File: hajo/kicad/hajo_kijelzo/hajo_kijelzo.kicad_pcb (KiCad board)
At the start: 2 copper layers, 69.2 x 89.5 mm, 26 parts, among them J1 Seetalk NG, J2 Batteries, J3 Terminator, J4 Conn_01x14, Q1 BC557, U1 MCP2562, U2 LF50CV, U3 LF33_TO220

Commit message: fix boards
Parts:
- Q1: footprint Package_TO_SOT_THT:TO-92_Inline -> Package_TO_SOT_THT:TO-92_Inline_Wide
- moved H2 0.50 mm to (18.6, 93.4)
- moved H4 0.50 mm to (76.9, 93.4)
- moved H1 0.25 mm to (76.9, 21.6)
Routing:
- net +3.3V: track 72.8 -> 75.9 mm
- net /L_BACK: track 26.4 -> 23.9 mm
- net Net-(Q1-B): track 5.08 -> 5.61 mm
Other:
- outline, holes or cut-outs redrawn
- board text added: "+"

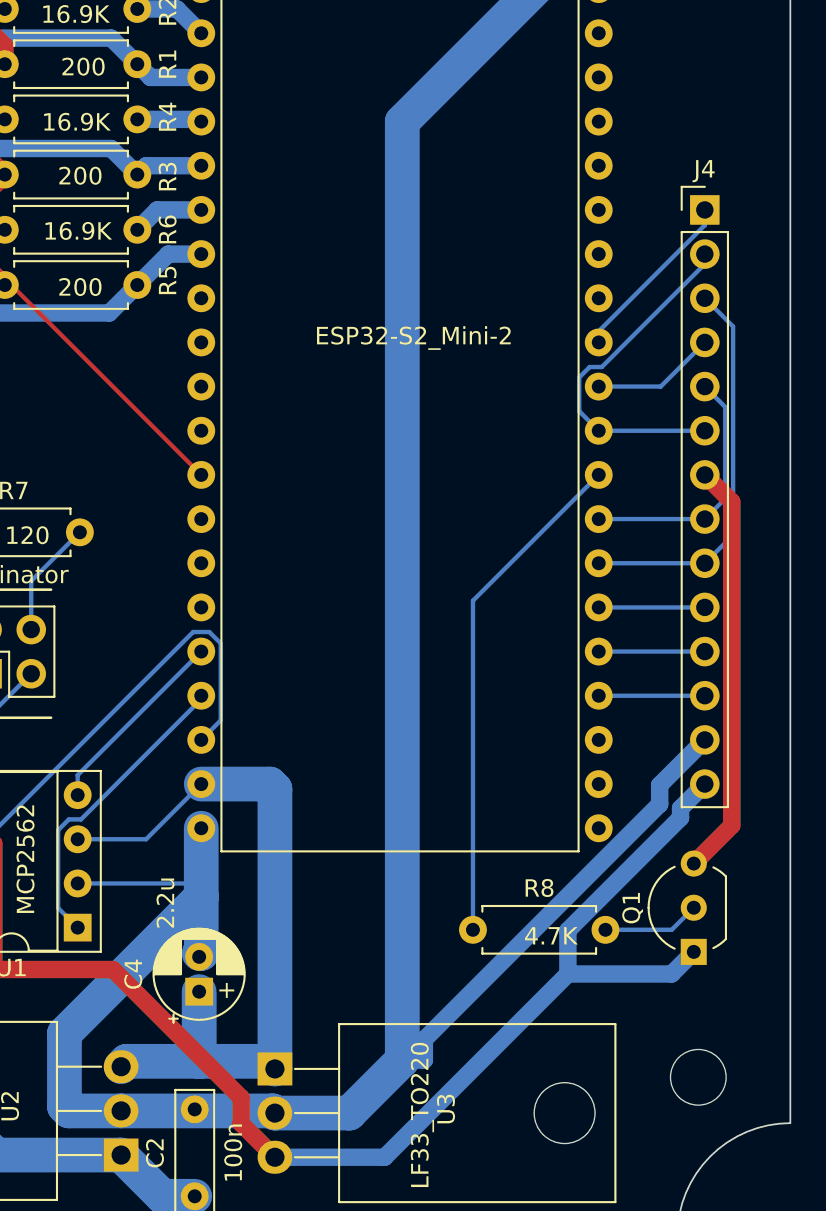
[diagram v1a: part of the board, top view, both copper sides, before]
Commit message: display pcb add capacitor, change R values
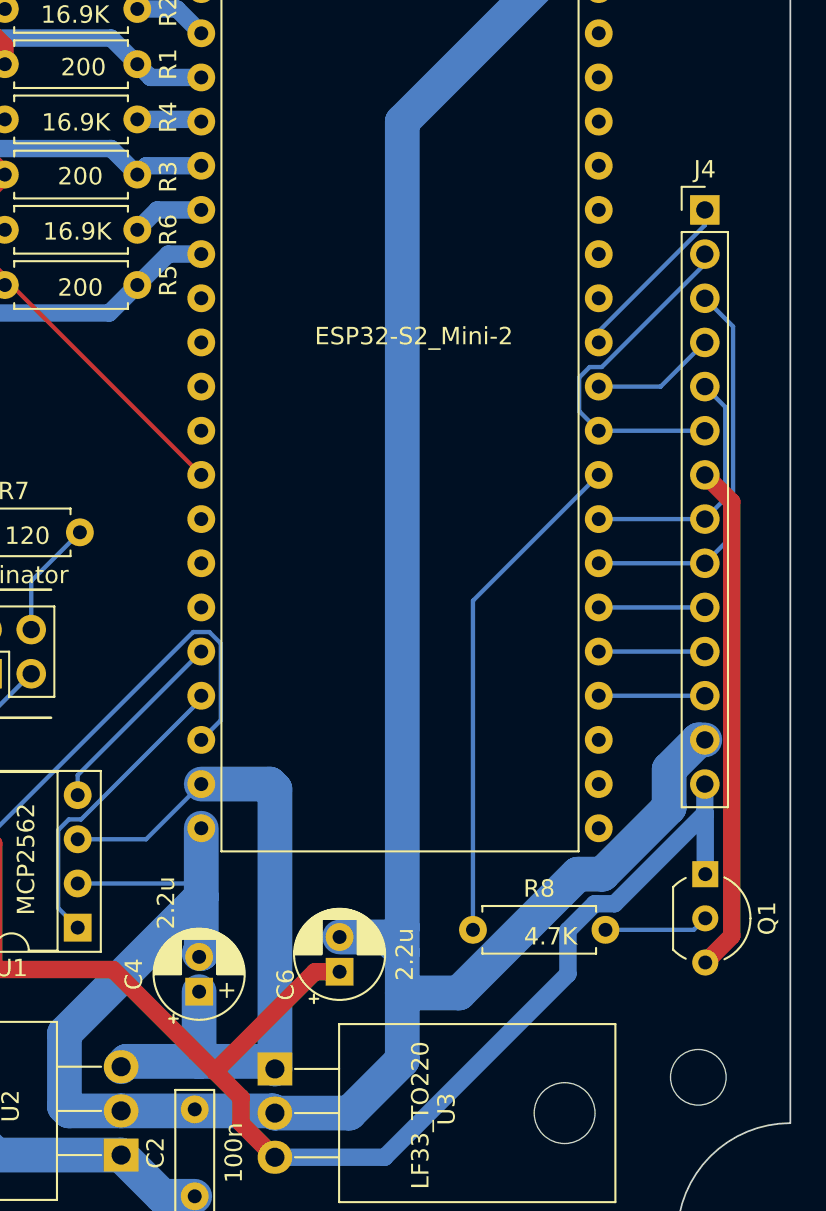
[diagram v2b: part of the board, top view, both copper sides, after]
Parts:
- added C6: 2.2u, Capacitor_THT:CP_Radial_D5.0mm_P2.00mm, F.Cu at (56.3, 87.3)
- moved Q1 4.52 mm to (77.3, 81.7), turned to -90 degrees
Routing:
- net +3.3V: track 75.9 -> 81.8 mm
- net /L_BACK: track 23.9 -> 29.3 mm
- net GND: track 288.3 -> 290.7 mm

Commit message: pcb changes
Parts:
- C1, C3, C5: footprint Capacitor_THT:C_Rect_L7.0mm_W2.0mm_P5.00mm -> Capacitor_THT:C_Rect_L4.0mm_W2.5mm_P2.50mm
- R1, R3, R5: value 200 -> 51.1
- R2, R4, R6: value 16.9K -> 806
- moved C1 5.68 mm to (34.0, 34.6)
- moved C3 5.63 mm to (34.1, 42.2)
- moved C5 5.46 mm to (34.1, 49.9)
- moved R5 4.95 mm to (37.1, 52.8)
- moved R6 4.95 mm to (44.7, 49.6)
- moved R4 3.64 mm to (44.6, 41.9)
- moved R3 3.64 mm to (37.0, 45.1)
- moved R1 2.29 mm to (36.9, 37.4)
- moved R2 2.29 mm to (44.5, 34.2)
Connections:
- A1 pad 10: unconnected-(A1-GPIO8/ADC1_7-Pad10) -> /ADC3_H
- A1 pad 11: unconnected-(A1-GPIO9/ADC1_8-Pad11) -> /ADC3_L
- A1 pad 4: /ADC1 -> /ADC1_H
- A1 pad 5: /DRV2 -> /ADC1_L
- A1 pad 6: /ADC2 -> /DRV2
- A1 pad 7: /DRV3 -> /ADC2_H
- A1 pad 8: /ADC3 -> /ADC2_L
- A1 pad 9: unconnected-(A1-GPIO7/ADC1_6-Pad9) -> /DRV3
- C1 pad 2: /ADC1 -> /ADC1_L
- C3 pad 2: /ADC2 -> /ADC2_L
- C5 pad 2: /ADC3 -> /ADC3_L
- J2 pad 1: /ADC3 -> /ADC3_L
- J2 pad 2: Net-(J2-Pin_2) -> /ADC3_H
- J2 pad 3: /ADC2 -> /ADC2_L
- J2 pad 4: Net-(J2-Pin_4) -> /ADC2_H
- J2 pad 5: /ADC1 -> /ADC1_L
- J2 pad 6: Net-(J2-Pin_6) -> /ADC1_H
- R1 pad 2: /ADC1 -> /ADC1_L
- R2 pad 2: Net-(J2-Pin_6) -> /ADC1_H
- R3 pad 2: /ADC2 -> /ADC2_L
- R4 pad 2: Net-(J2-Pin_4) -> /ADC2_H
- R5 pad 2: /ADC3 -> /ADC3_L
- R6 pad 2: Net-(J2-Pin_2) -> /ADC3_H
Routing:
- net /ADC3: track 24.7 -> 0.00 mm
- net /ADC3_L: track 0.00 -> 23.5 mm
- net /ADC2: track 23.5 -> 0.00 mm
- net /ADC1_L: track 0.00 -> 22.5 mm
- net /ADC2_L: track 0.00 -> 22.4 mm
- net /ADC3_H: track 0.00 -> 22.4 mm
- net /ADC1_H: track 0.00 -> 22.3 mm
- net /ADC1: track 22.0 -> 0.00 mm
- net /ADC2_H: track 0.00 -> 21.3 mm
- net Net-(J2-Pin_2): track 11.5 -> 0.00 mm
- net Net-(J2-Pin_4): track 9.94 -> 0.00 mm
- net Net-(J2-Pin_6): track 9.42 -> 0.00 mm
- net GND: track 290.7 -> 296.5 mm

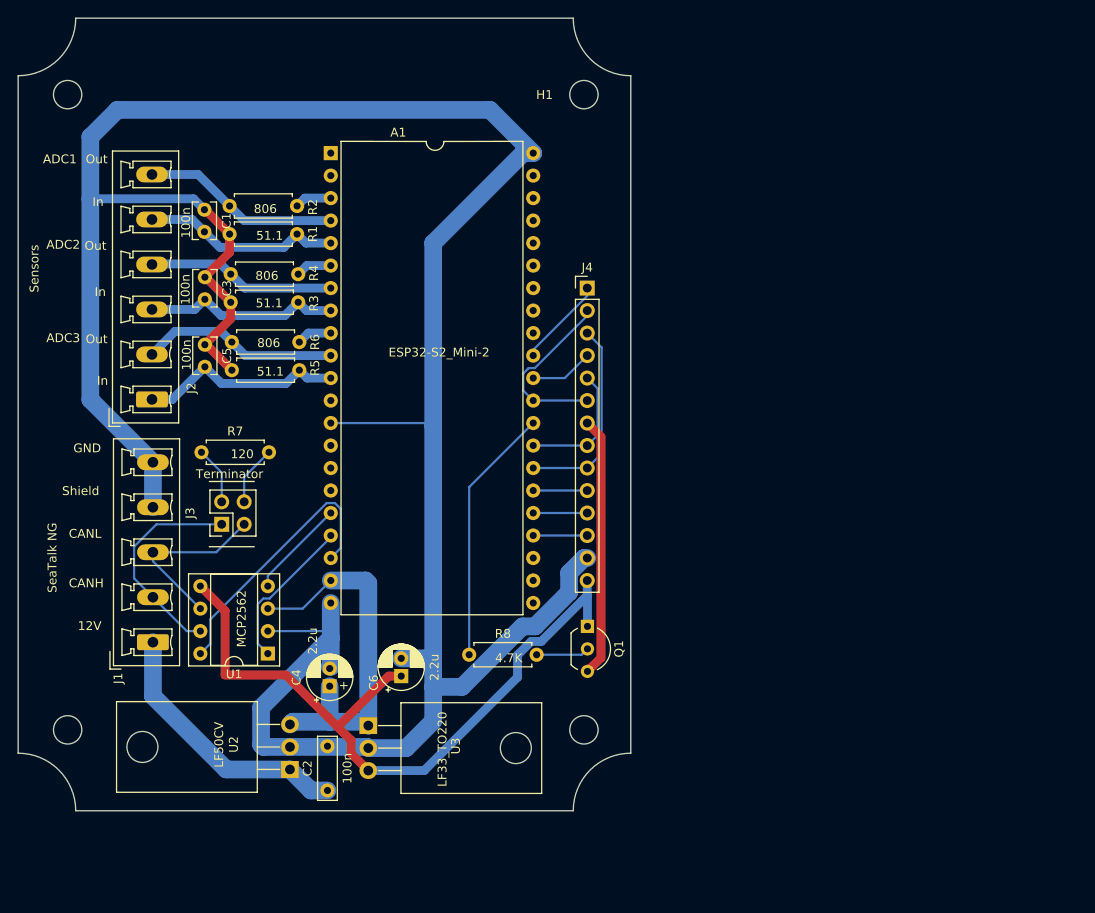
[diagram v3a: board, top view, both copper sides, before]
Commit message: kijelzo on new board
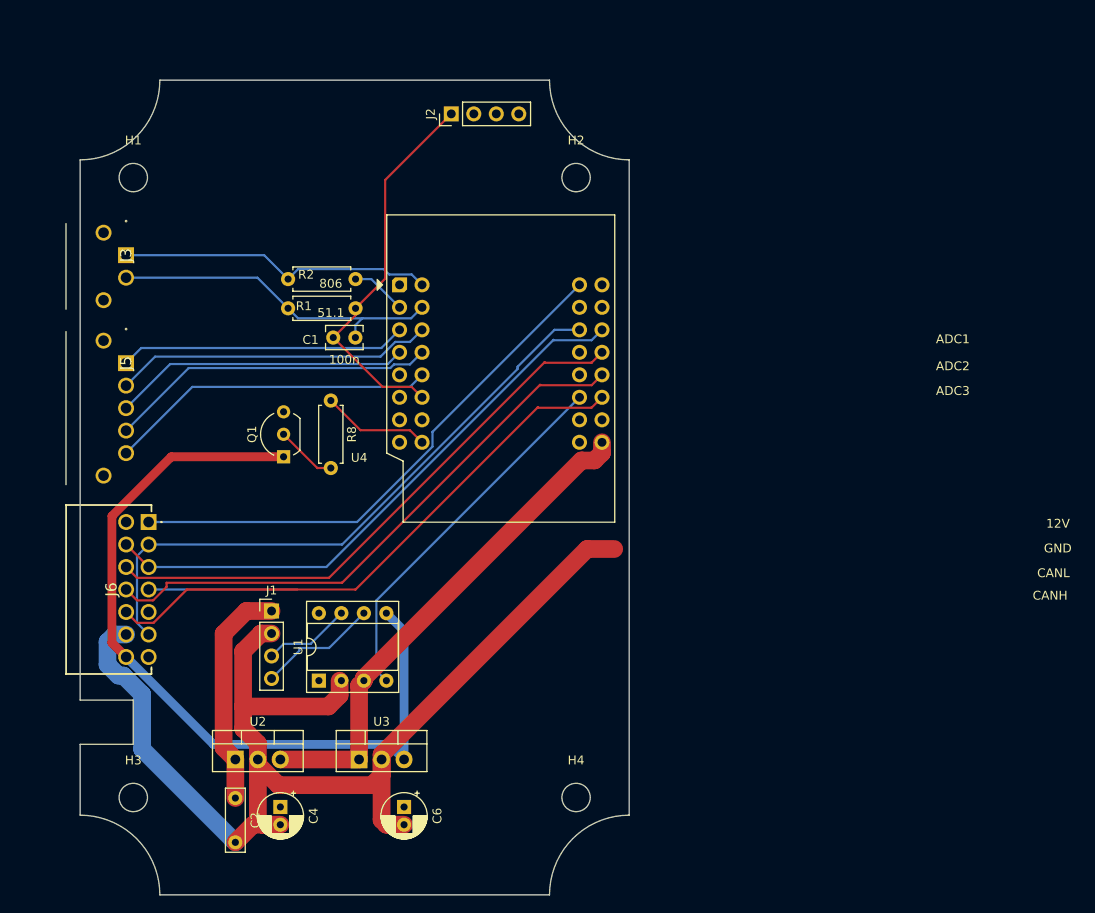
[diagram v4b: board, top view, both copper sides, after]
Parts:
- removed A1: ESP32-S2_Mini-2, own:DIP-42_W15.24mm
- removed C3, C5: 100n, Capacitor_THT:C_Rect_L4.0mm_W2.5mm_P2.50mm
- removed J4: Conn_01x14, Connector_PinHeader_2.54mm:PinHeader_1x14_P2.54mm_Vertical
- removed R3, R5: 51.1, Resistor_THT:R_Axial_DIN0207_L6.3mm_D2.5mm_P7.62mm_Horizontal
- removed R4, R6: 806, Resistor_THT:R_Axial_DIN0207_L6.3mm_D2.5mm_P7.62mm_Horizontal
- removed R7: 120, Resistor_THT:R_Axial_DIN0207_L6.3mm_D2.5mm_P7.62mm_Horizontal
- added J5: Water, SamacSys_Parts:1821274, F.Cu at (25.2, 52.0)
- added J6: Display, SamacSys_Parts:1844772, F.Cu at (27.7, 69.9)
- added U4: WeMos_S2_mini, own:WEMOS_S2_mini_traced, F.Cu at (56.1, 43.1)
- J1: value Seetalk NG -> SeaTalk NG; footprint Connector_Phoenix_MC_HighVoltage:PhoenixContact_MCV_1,5_5-G-5.08_1x05_P5.08mm_Vertical -> Connector_PinHeader_2.54mm:PinHeader_1x04_P2.54mm_Vertical
- J2: value Batteries -> Debug; footprint Connector_Phoenix_MC_HighVoltage:PhoenixContact_MCV_1,5_6-G-5.08_1x06_P5.08mm_Vertical -> Connector_PinHeader_2.54mm:PinHeader_1x04_P2.54mm_Vertical
- J3: value Terminator -> Fuel; footprint Connector_PinHeader_2.54mm:PinHeader_2x02_P2.54mm_Vertical -> SamacSys_Parts:1821245
- U2, U3: footprint Package_TO_SOT_THT:TO-220-3_Horizontal_TabDown -> Package_TO_SOT_THT:TO-220-3_Vertical
- moved H2 84.8 mm to (76.0, 31.0)
- moved H3 79.7 mm to (26.0, 101.0)
- moved H1 51.7 mm to (26.0, 31.0)
- moved J2 46.7 mm to (61.9, 23.8)
- moved Q1 39.3 mm to (43.0, 62.5), turned to 90 degrees
- moved R8 32.7 mm to (48.3, 56.2), turned to -90 degrees
- moved J3 32.3 mm to (25.2, 39.8), turned to -90 degrees
- moved C1 20.5 mm to (48.6, 49.1), turned to 0 degrees
- moved R1 16.5 mm to (51.1, 45.8), turned to 180 degrees
- moved C6 14.8 mm to (56.6, 102.1), turned to -90 degrees
- moved C4 14.7 mm to (42.6, 102.1), turned to -90 degrees
- moved J1 13.8 mm to (41.6, 79.9), turned to 0 degrees
- moved R2 10.6 mm to (51.1, 42.5)
- moved C2 10.4 mm to (37.5, 101.1), turned to -90 degrees
- moved H4 7.69 mm to (76.0, 101.0)
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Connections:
- J1 pad 2: /CANH -> GND
- J1 pad 3: /CANL -> /CANH
- J1 pad 4: GND -> /CANL
- J2 pad 1: /ADC3_L -> GND
- J2 pad 2: /ADC3_H -> unconnected-(J2-Pin_2-Pad2)
- J2 pad 3: /ADC2_L -> /DebugTX
- J2 pad 4: /ADC2_H -> /DebugRX
- J3 pad 1: /CANH -> /ADC1_H
- J3 pad 2: Net-(J3-Pin_2) -> /ADC1_L
- J3 pad 3: /CANL -> (no net)
- J3 pad 4: Net-(J3-Pin_4) -> (no net)
- R8 pad 1: Net-(A1-GPIO36) -> /LED
- U1 pad 1: /TXD -> /CanTX
- U1 pad 4: /RXD -> /CanRX
- U1 pad 8: /STBY -> /CanStdby
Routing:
- net GND: track 296.5 -> 182.3 mm
- net /L_RESET: track 6.10 -> 65.1 mm
- net /L_DC: track 6.10 -> 64.8 mm
- net /L_CS: track 6.10 -> 64.8 mm
- net /T_IRQ: track 10.1 -> 60.7 mm
- net /SDO: track 20.1 -> 70.1 mm
- net /SDI: track 22.7 -> 65.9 mm
- net /CanRX: track 0.00 -> 42.0 mm
- net /Water1: track 0.00 -> 37.1 mm
- net /Water0: track 0.00 -> 37.1 mm
- net /Water3: track 0.00 -> 36.0 mm
- net /Water2: track 0.00 -> 33.5 mm
- net /Water4: track 0.00 -> 32.4 mm
- net /STBY: track 30.8 -> 0.00 mm
- net /L_BACK: track 29.3 -> 0.00 mm
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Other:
- board size 69.2 x 89.5 mm -> 62 x 92 mm
- board text removed: "+"
- board text removed: "In"
- board text removed: "Out"
- board text removed: "SeaTalk NG"
- board text removed: "Sensors"
- board text removed: "Shield"
- board text removed: "Terminator"

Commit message: pcv rework
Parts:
- moved R2 6.35 mm to (45.2, 40.2)
- moved C1 5.98 mm to (42.6, 49.3)
- moved R1 5.98 mm to (45.1, 46.0)
- moved U4 4.50 mm to (53.1, 46.5)
- moved Q1 4.22 mm to (38.8, 62.7)
- moved R8 4.22 mm to (44.1, 56.3)
- moved J6 0.76 mm to (27.7, 69.1)
- moved J5 0.60 mm to (25.2, 51.4)
- moved J3 0.35 mm to (25.2, 39.4)
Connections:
- J2 pad 3: /DebugTX -> /DebugRX
- J2 pad 4: /DebugRX -> /DebugTX
- U1 pad 8: /CanStdby -> GND
- U4 pad 11: /L_CS -> /CanRX
- U4 pad 12: /L_RESET -> /SCK
- U4 pad 13: /L_DC -> /T_CS
- U4 pad 15: /SCK -> /SDO
- U4 pad 16: /LED -> /DebugTX
- U4 pad 17: /ADC1_H -> unconnected-(U4-GPIO1-Pad17)
- U4 pad 18: /ADC1_L -> GND
- U4 pad 19: /Water3 -> unconnected-(U4-GPIO4-Pad19)
- U4 pad 20: /Water1 -> /Water4
- U4 pad 21: /Water0 -> /Water2
- U4 pad 22: GND -> unconnected-(U4-GPIO10-Pad22)
- U4 pad 23: unconnected-(U4-GPIO13-Pad23) -> /LED
- U4 pad 24: /LED -> unconnected-(U4-GPIO14-Pad24)
- U4 pad 27: /CanRX -> /CanTX
- U4 pad 28: /CanTX -> /L_CS
- U4 pad 29: /CanStdby -> /L_RESET
- U4 pad 3: /Water4 -> /ADC1_H
- U4 pad 30: /SDO -> /L_DC
- U4 pad 31: /T_CS -> /T_IRQ
- U4 pad 32: /T_IRQ -> /DebugRX
- U4 pad 4: /Water2 -> /ADC1_L
- U4 pad 5: unconnected-(U4-GPIO9-Pad5) -> /Water3
- U4 pad 6: unconnected-(U4-GPIO11-Pad6) -> /Water1
- U4 pad 7: unconnected-(U4-GPIO12-Pad7) -> /Water0
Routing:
- net GND: track 182.3 -> 281.2 mm
- net /SCK: track 0.00 -> 70.9 mm
- net /T_CS: track 16.8 -> 57.6 mm
- net /CanTX: track 0.00 -> 39.6 mm
- net /L_BACK: track 0.00 -> 32.7 mm
- net /DebugRX: track 0.00 -> 30.3 mm
- net /DebugTX: track 0.00 -> 28.0 mm
- net /DRV1: track 6.29 -> 14.8 mm
- net +3.3V: track 92.2 -> 84.7 mm
- net /L_RESET: track 65.1 -> 57.6 mm
- net /L_DC: track 64.8 -> 57.6 mm
- net /L_CS: track 64.8 -> 57.6 mm
- net /T_IRQ: track 60.7 -> 54.0 mm
- net /Water3: track 36.0 -> 29.9 mm
- net +5V: track 56.9 -> 62.1 mm
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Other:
- outline, holes or cut-outs redrawn
- board text added: "FuelH"
- board text added: "FuelL"
- board text added: "NC"
- board text added: "RXD"
- board text added: "TXD"
- board text added: "Water0"
- board text added: "Water1"
- board text added: "Water2"
- board text added: "Water3"
- board text added: "Water4"
- board text removed: "ADC1"
- board text removed: "ADC2"
- board text removed: "ADC3"
